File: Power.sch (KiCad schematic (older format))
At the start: 11 parts

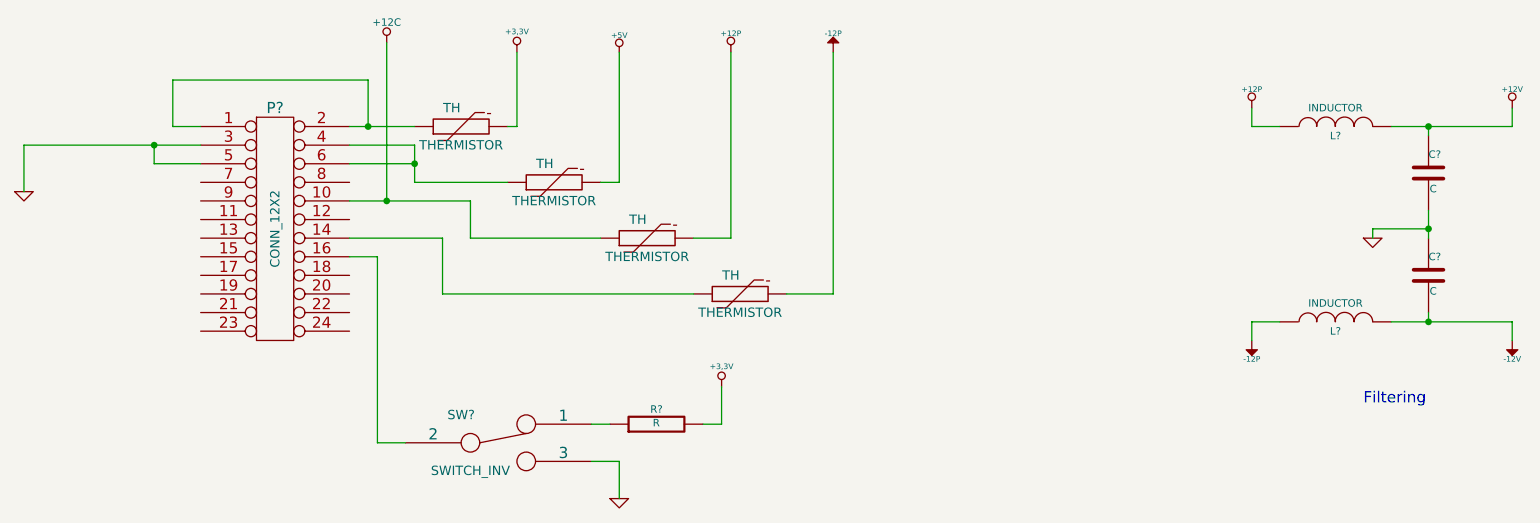
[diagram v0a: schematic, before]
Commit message: associating and placing relay module
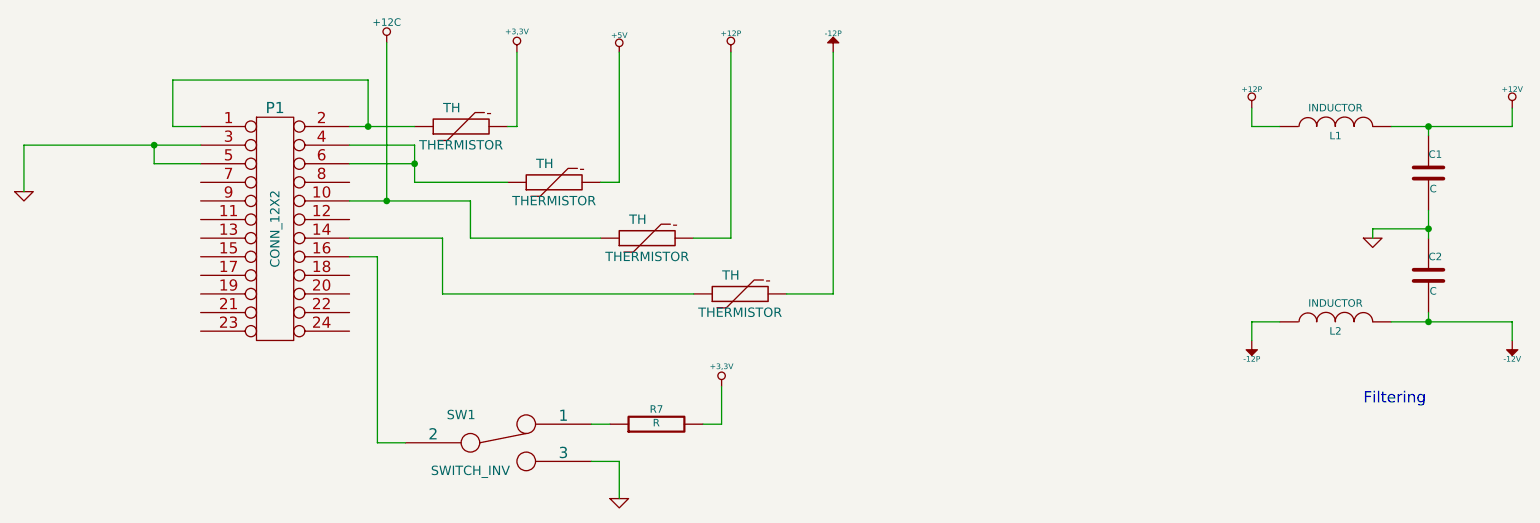
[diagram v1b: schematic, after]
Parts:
- gave numbers to parts that had none: 11
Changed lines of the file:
@@
 Sheet 3 9
 Title ""
-Date "10 feb 2014"
+Date "22 feb 2014"
 Rev ""
 Comp ""
@@
 $EndDescr
 $Comp
-L CONN_12X2 P?
+L CONN_12X2 P1
 U 1 1 52F3A9AC
 P 2350 2100
-F 0 "P?" H 2350 2750 60  0000 C CNN
+F 0 "P1" H 2350 2750 60  0000 C CNN
 F 1 "CONN_12X2" V 2350 2100 50  0000 C CNN
 F 2 "" H 2350 2100 60  0000 C CNN
@@
 $EndComp
 $Comp
-L GND #PWR?
+L GND #PWR03
 U 1 1 52F3A9C1
 P 1000 1900
-F 0 "#PWR?" H 1000 1900 30  0001 C CNN
+F 0 "#PWR03" H 1000 1900 30  0001 C CNN
 F 1 "GND" H 1000 1830 30  0001 C CNN
 F 2 "" H 1000 1900 60  0000 C CNN
@@
 $EndComp
 $Comp
-L +3,3V #PWR?
+L +3,3V #PWR04
 U 1 1 52F3A9DA
 P 3650 1150
-F 0 "#PWR?" H 3650 1110 30  0001 C CNN
+F 0 "#PWR04" H 3650 1110 30  0001 C CNN
 F 1 "+3,3V" H 3650 1260 30  0000 C CNN
 F 2 "" H 3650 1150 60  0000 C CNN
@@
 $EndComp
 $Comp
-L +5V #PWR?
+L +5V #PWR05
 U 1 1 52F3A9E9
 P 4200 1150
-F 0 "#PWR?" H 4200 1240 20  0001 C CNN
+F 0 "#PWR05" H 4200 1240 20  0001 C CNN
 F 1 "+5V" H 4200 1240 30  0000 C CNN
 F 2 "" H 4200 1150 60  0000 C CNN
@@
 	5350 2450 5350 1150
 $Comp
-L +12P #PWR?
+L +12P #PWR06
 U 1 1 52F3AB31
 P 4800 1150
-F 0 "#PWR?" H 4800 1120 30  0001 C CNN
+F 0 "#PWR06" H 4800 1120 30  0001 C CNN
 F 1 "+12P" H 4800 1250 30  0000 C CNN
 F 2 "" H 4800 1150 60  0000 C CNN
@@
 Connection ~ 2850 1550
 $Comp
-L -12P #PWR?
+L -12P #PWR07
 U 1 1 52F3ABC6
 P 5350 1150
-F 0 "#PWR?" H 5350 1280 20  0001 C CNN
+F 0 "#PWR07" H 5350 1280 20  0001 C CNN
 F 1 "-12P" H 5350 1250 30  0000 C CNN
 F 2 "" H 5350 1150 60  0000 C CNN
@@
 	2750 2250 2900 2250
 $Comp
-L GND #PWR?
+L GND #PWR08
 U 1 1 52F3AC14
 P 4200 3550
-F 0 "#PWR?" H 4200 3550 30  0001 C CNN
+F 0 "#PWR08" H 4200 3550 30  0001 C CNN
 F 1 "GND" H 4200 3480 30  0001 C CNN
 F 2 "" H 4200 3550 60  0000 C CNN
@@
 $EndComp
 $Comp
-L R R?
+L R R7
 U 1 1 52F3AC3E
 P 4400 3150
-F 0 "R?" V 4480 3150 40  0000 C CNN
+F 0 "R7" V 4480 3150 40  0000 C CNN
 F 1 "R" V 4407 3151 40  0000 C CNN
 F 2 "~" V 4330 3150 30  0000 C CNN
@@
 $EndComp
 $Comp
-L SWITCH_INV SW?
+L SWITCH_INV SW1
 U 1 1 52F3AC4D
 P 3550 3250
-F 0 "SW?" H 3350 3400 50  0000 C CNN
+F 0 "SW1" H 3350 3400 50  0000 C CNN
 F 1 "SWITCH_INV" H 3400 3100 50  0000 C CNN
 F 2 "~" H 3550 3250 60  0000 C CNN
@@
 	4750 3150 4750 2950
 $Comp
-L +3,3V #PWR?
+L +3,3V #PWR09
 U 1 1 52F3ACFA
 P 4750 2950
-F 0 "#PWR?" H 4750 2910 30  0001 C CNN
+F 0 "#PWR09" H 4750 2910 30  0001 C CNN
 F 1 "+3,3V" H 4750 3060 30  0000 C CNN
 F 2 "" H 4750 2950 60  0000 C CNN
@@
 $EndComp
 $Comp
-L +12P #PWR?
+L +12P #PWR010
 U 1 1 52F3AD00
 P 7600 1450
-F 0 "#PWR?" H 7600 1420 30  0001 C CNN
+F 0 "#PWR010" H 7600 1420 30  0001 C CNN
 F 1 "+12P" H 7600 1550 30  0000 C CNN
 F 2 "" H 7600 1450 60  0000 C CNN
@@
 $EndComp
 $Comp
-L -12P #PWR?
+L -12P #PWR011
 U 1 1 52F3AD06
 P 7600 2700
-F 0 "#PWR?" H 7600 2830 20  0001 C CNN
+F 0 "#PWR011" H 7600 2830 20  0001 C CNN
 F 1 "-12P" H 7600 2800 30  0000 C CNN
 F 2 "" H 7600 2700 60  0000 C CNN
@@
 $EndComp
 $Comp
-L GND #PWR?
+L GND #PWR012
 U 1 1 52F3AD0C
 P 8250 2150
-F 0 "#PWR?" H 8250 2150 30  0001 C CNN
+F 0 "#PWR012" H 8250 2150 30  0001 C CNN
 F 1 "GND" H 8250 2080 30  0001 C CNN
 F 2 "" H 8250 2150 60  0000 C CNN
@@
 $EndComp
 $Comp
-L INDUCTOR L?
+L INDUCTOR L2
 U 1 1 52F3AD14
 P 8050 2600
-F 0 "L?" V 8000 2600 40  0000 C CNN
+F 0 "L2" V 8000 2600 40  0000 C CNN
 F 1 "INDUCTOR" V 8150 2600 40  0000 C CNN
 F 2 "~" H 8050 2600 60  0000 C CNN
@@
 $EndComp
 $Comp
-L INDUCTOR L?
+L INDUCTOR L1
 U 1 1 52F3AD23
 P 8050 1550
-F 0 "L?" V 8000 1550 40  0000 C CNN
+F 0 "L1" V 8000 1550 40  0000 C CNN
 F 1 "INDUCTOR" V 8150 1550 40  0000 C CNN
 F 2 "~" H 8050 1550 60  0000 C CNN
@@
 $EndComp
 $Comp
-L C C?
+L C C1
 U 1 1 52F3AD32
 P 8550 1800
-F 0 "C?" H 8550 1900 40  0000 L CNN
+F 0 "C1" H 8550 1900 40  0000 L CNN
 F 1 "C" H 8556 1715 40  0000 L CNN
 F 2 "~" H 8588 1650 30  0000 C CNN
@@
 $EndComp
 $Comp
-L C C?
+L C C2
 U 1 1 52F3AD49
 P 8550 2350
-F 0 "C?" H 8550 2450 40  0000 L CNN
+F 0 "C2" H 8550 2450 40  0000 L CNN
 F 1 "C" H 8556 2265 40  0000 L CNN
 F 2 "~" H 8588 2200 30  0000 C CNN
@@
 Connection ~ 8550 2100
 $Comp
-L -12V #PWR?
+L -12V #PWR013
 U 1 1 52F3AE74
 P 9000 2700
-F 0 "#PWR?" H 9000 2830 20  0001 C CNN
+F 0 "#PWR013" H 9000 2830 20  0001 C CNN
 F 1 "-12V" H 9000 2800 30  0000 C CNN
 F 2 "" H 9000 2700 60  0000 C CNN
@@
 $EndComp
 $Comp
-L +12V #PWR?
+L +12V #PWR014
 U 1 1 52F3AE83
 P 9000 1450
-F 0 "#PWR?" H 9000 1400 20  0001 C CNN
+F 0 "#PWR014" H 9000 1400 20  0001 C CNN
 F 1 "+12V" H 9000 1550 30  0000 C CNN
 F 2 "" H 9000 1450 60  0000 C CNN
@@
 Connection ~ 2950 1950
 $Comp
-L +12C #PWR?
+L +12C #PWR015
 U 1 1 52F8F8DF
 P 2950 1100
-F 0 "#PWR?" H 3000 1150 60  0001 C CNN
+F 0 "#PWR015" H 3000 1150 60  0001 C CNN
 F 1 "+12C" H 2950 1100 60  0001 C CNN
 F 2 "" H 2950 1100 60  0000 C CNN
@@
 $EndComp
 $Comp
-L THERMISTOR TH?
+L THERMISTOR TH1
 U 1 1 52F8FA4B
 P 3350 1550
-F 0 "TH?" H 3400 1600 60  0001 C CNN
+F 0 "TH1" H 3400 1600 60  0001 C CNN
 F 1 "THERMISTOR" H 3350 1550 60  0001 C CNN
 F 2 "~" H 3350 1550 60  0000 C CNN
@@
 $EndComp
 $Comp
-L THERMISTOR TH?
+L THERMISTOR TH2
 U 1 1 52F8FA72
 P 3850 1850
-F 0 "TH?" H 3900 1900 60  0001 C CNN
+F 0 "TH2" H 3900 1900 60  0001 C CNN
 F 1 "THERMISTOR" H 3850 1850 60  0001 C CNN
 F 2 "~" H 3850 1850 60  0000 C CNN
@@
 $EndComp
 $Comp
-L THERMISTOR TH?
+L THERMISTOR TH3
 U 1 1 52F8FA7B
 P 4350 2150
-F 0 "TH?" H 4400 2200 60  0001 C CNN
+F 0 "TH3" H 4400 2200 60  0001 C CNN
 F 1 "THERMISTOR" H 4350 2150 60  0001 C CNN
 F 2 "~" H 4350 2150 60  0000 C CNN
@@
 $EndComp
 $Comp
-L THERMISTOR TH?
+L THERMISTOR TH4
 U 1 1 52F8FA84
 P 4850 2450
-F 0 "TH?" H 4900 2500 60  0001 C CNN
+F 0 "TH4" H 4900 2500 60  0001 C CNN
 F 1 "THERMISTOR" H 4850 2450 60  0001 C CNN
 F 2 "~" H 4850 2450 60  0000 C CNN
